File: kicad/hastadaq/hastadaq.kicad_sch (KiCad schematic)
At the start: 38 parts, among them J1 IMU via Qwiic breakout (The P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, J10 SBUS IN (RC receiver): GND, V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, J2 GAUGE BOARD LOOM (J_I2C): GND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, J3 ENC1 SPI port: MT6835 (pitch)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, J4 ENC2 SPI port: MT6835 / Orbis, J5 ENC3 SPI port: MT6835 / Orbis, J6 ENC4 SPI port: generic SPI de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, J7 SBUS servo header 3x6 (6 plug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, J8 Main supply cable (2x4): VSUP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, J9 TRIG_OUT pull-up sel., Q1 2N3904 NPN (TO-92, pin 1 E, 2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, U1 Pimoroni Pico Plus 2 (header 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, U2 Pololu D42V55F8 8.4V 5A buck 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, U3 SparkFun BabyBuck 5V (AP63357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, U4 PC817 opto (TRIG_IN)

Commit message: Schematics: fuse removed, plain headers, real parts chosen; gauge board LDO/caps; hand-off docs
- Main board: no fuse (+12V straight from the supply connector), every connector a
  plain 0.1 in header, plain test pads, FOD817A opto, chosen capacitor footprints
- Gauge board: MCP1700-3302E/TO LDO (pin 1 GND, 2 VIN, 3 VOUT), tantalum output cap,
  Vishay K-series 100 nF with 2.5 mm pitch, DNP flags on the filter caps, test points,
  pass-through loom header, redundant ADC decoupling removed
- Docs: PCB_BRIEF.md/PCB_BRIEF_GAUGE.md rewritten with a status and hand-off section,
  new PARTS_TO_SELECT.md (RS numbers, dimensions, open items), README updated,
  BabyBuck EN and ADS122C04 pull-up/address facts recorded from the data sheets

Co-Authored-By: Claude Sonnet 5.5 <noreply@anthropic.com>
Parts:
- removed F1: Fuse T3.15A 5x20mm time-delay, Fuse:Fuseholder_Clip-5x20mm_Keystone_3517_Inline_P23.11x6.76mm_D1.70mm_Horizontal, symbol HastaDAQ:Fuse
- C1: value 100uF input bulk (>=25V) -> 100uF 25V input bulk (Panasonic ECA1EM101); footprint Capacitor_THT:CP_Radial_D8.0mm_P3.50mm -> Capacitor_THT:CP_Radial_D6.3mm_P2.50mm
- C2: value 470-1000uF servo bulk (>=16V) -> 470uF 16V servo bulk (Panasonic EEUFR1C471); footprint Capacitor_THT:CP_Radial_D10.0mm_P5.00mm -> Capacitor_THT:CP_Radial_D8.0mm_P3.50mm
- C3: value 100uF 5V bulk (>=10V) -> 100uF 10V 5V bulk (RS PRO LHK 5x7); footprint Capacitor_THT:CP_Radial_D6.3mm_P2.50mm -> Capacitor_THT:CP_Radial_D5.0mm_P2.00mm
- J1: footprint HastaDAQ:Qwiic_Breakout_1x4_Socket -> Connector_PinHeader_2.54mm:PinHeader_1x04_P2.54mm_Vertical
- J3, J4, J5, J6, J8: footprint Connector_IDC:IDC-Header_2x04_P2.54mm_Vertical -> Connector_PinHeader_2.54mm:PinHeader_2x04_P2.54mm_Vertical
- TP1, TP2: footprint TestPoint:TestPoint_THTPad_D2.0mm_Drill1.0mm -> TestPoint:TestPoint_Pad_D2.0mm
- U4: value PC817 opto (TRIG_IN) -> FOD817A opto (TRIG_IN)
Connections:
- net +12V_IN is gone; now on net +12V: J8.1 (VSUPPLY), J8.8 (VSUPPLY)
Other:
- note added: "PWR_FLAG: marks nets supplied through the supply connector (+12V, GND) and the Schottky (+5V_VSYS)"
- note added: "TEST POINTS (plain 2.0 mm pads): two GND pads for a scope clip (near the supply and near the Pico). Rails and signals are probed at component leads and header pins (C1/C2/C3, D1, Pico pins 36/39)."
- note removed: "PWR_FLAG: marks nets supplied through the supply connector (+12V_IN, GND), the fuse (+12V) and the Schottky (+5V_VSYS)"
- note removed: "TEST POINTS (2.0 mm through-hole pads): two GND pads for a scope clip (near the supply and near the Pico). Rails and signals are probed at component leads and header pins (fuse clips, C5/C6/C7, D1, Pico pins 36/39)."

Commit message: Schematics: shunt-safe J9, SBUS IN on +5V with zener, 20 V max note; publish tool
- J9 TRIG_OUT pull-up select is now a 1x5 header (rails separated by PU pins) so a shunt cannot join two rails
- SBUS IN is powered from +5V (Futaba R3008SB is 4.8-7.4 V) with a 5.1 V zener clamp (D4); R14 pull-down left unfitted first (RP2350 E9)
- Supply maximum 20 V documented (C1 25 V rating); no TVS
- Gauge brief: plug-order correction, stray L1 row removed
- kicad/tools/publish.py snapshots both schematics into kicad/releases/<name>/ for PCB layout
- PDFs/PNGs re-exported

Co-Authored-By: Claude Sonnet 5.5 <noreply@anthropic.com>
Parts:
- removed J9: TRIG_OUT pull-up sel., Connector_PinHeader_2.54mm:PinHeader_2x03_P2.54mm_Vertical, symbol HastaDAQ:Header2x03_PU_SEL
- added D4: 5.1V zener (BZX55C5V1) SBUS IN clamp, Diode_THT:D_DO-35_SOD27_P7.62mm_Horizontal, symbol HastaDAQ:D_Zener
- added J9: TRIG_OUT pull-up (1x5), Connector_PinHeader_2.54mm:PinHeader_1x05_P2.54mm_Vertical, symbol HastaDAQ:Header1x05_3V3pPUp5VpPUp12V
- R14: value 10k pull-down -> 10k pull-down (DNP at first)
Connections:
- net +12V: now also J9.5 (12V)
- net +3V3: now also J9.1 (3V3)
- net +5V: now also J10.2 (V), J9.3 (5V)
- net GND: now also D4.A
- net SBUS_IN_GPIO: now also D4.K
- net TRIG_PU: now also J9.2 (PU), J9.4 (PU)
- net VSERVO: no longer J10.2 (V)
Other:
- note added: "SBUS IN: RC-receiver pass-through (plug order GND, V, SIG). V = +5V (NOT VSERVO: the Futaba R3008SB takes 4.8-7.4 V, so 8.4 V would overstress it; check any other receiver's range). SIG -> 1k -> GP1 (UART0 RX); 5.1 V zener clamps a receiver that outputs more than 5.1 V (about 100 pF at 100 kbaud: harmless). 10k pull-down R: leave UNFITTED on the first trial; RP2350 erratum E9 can hold a pin with 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"
- note added: "Shunt pins 1-2 (3V3), 2-3 (5V) or 4-5 (12V) to pull TRIG_OUT up to that rail; fit none if the receiver has its own pull-up. Pins 2 and 4 are both TRIG_PU. Fit ONE shunt only (two shunts could join rails). Pull-up current: 3.3 V ~2 mA, 5 V ~3 mA, 12 V ~7 mA (enough for a 6.5 mA opto input such as MPS4200). 24 V receivers: no jumper, add an external 24 V pull-up in the harness. 3V3 for eSync 2 high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"
- note removed: "Jumper a row (3V3 / 5V / 12V) to pull TRIG_OUT up to that rail; remove it if the receiver has its own pull-up. Pull-up current: 3.3 V ~2 mA, 5 V ~3 mA, 12 V ~7 mA (enough for a 6.5 mA opto input such as MPS4200). 24 V receivers: no jumper, add an external 24 V pull-up in the harness. 3V3 for eSync 2 high-Z ports (3.3 V max)."
- note removed: "SBUS IN: RC-receiver pass-through (plug order GND, V, SIG). V = VSERVO 8.4 V -- check the receiver's max supply. SIG -> 1k -> GP1 (UART0 RX), 10k to GND."

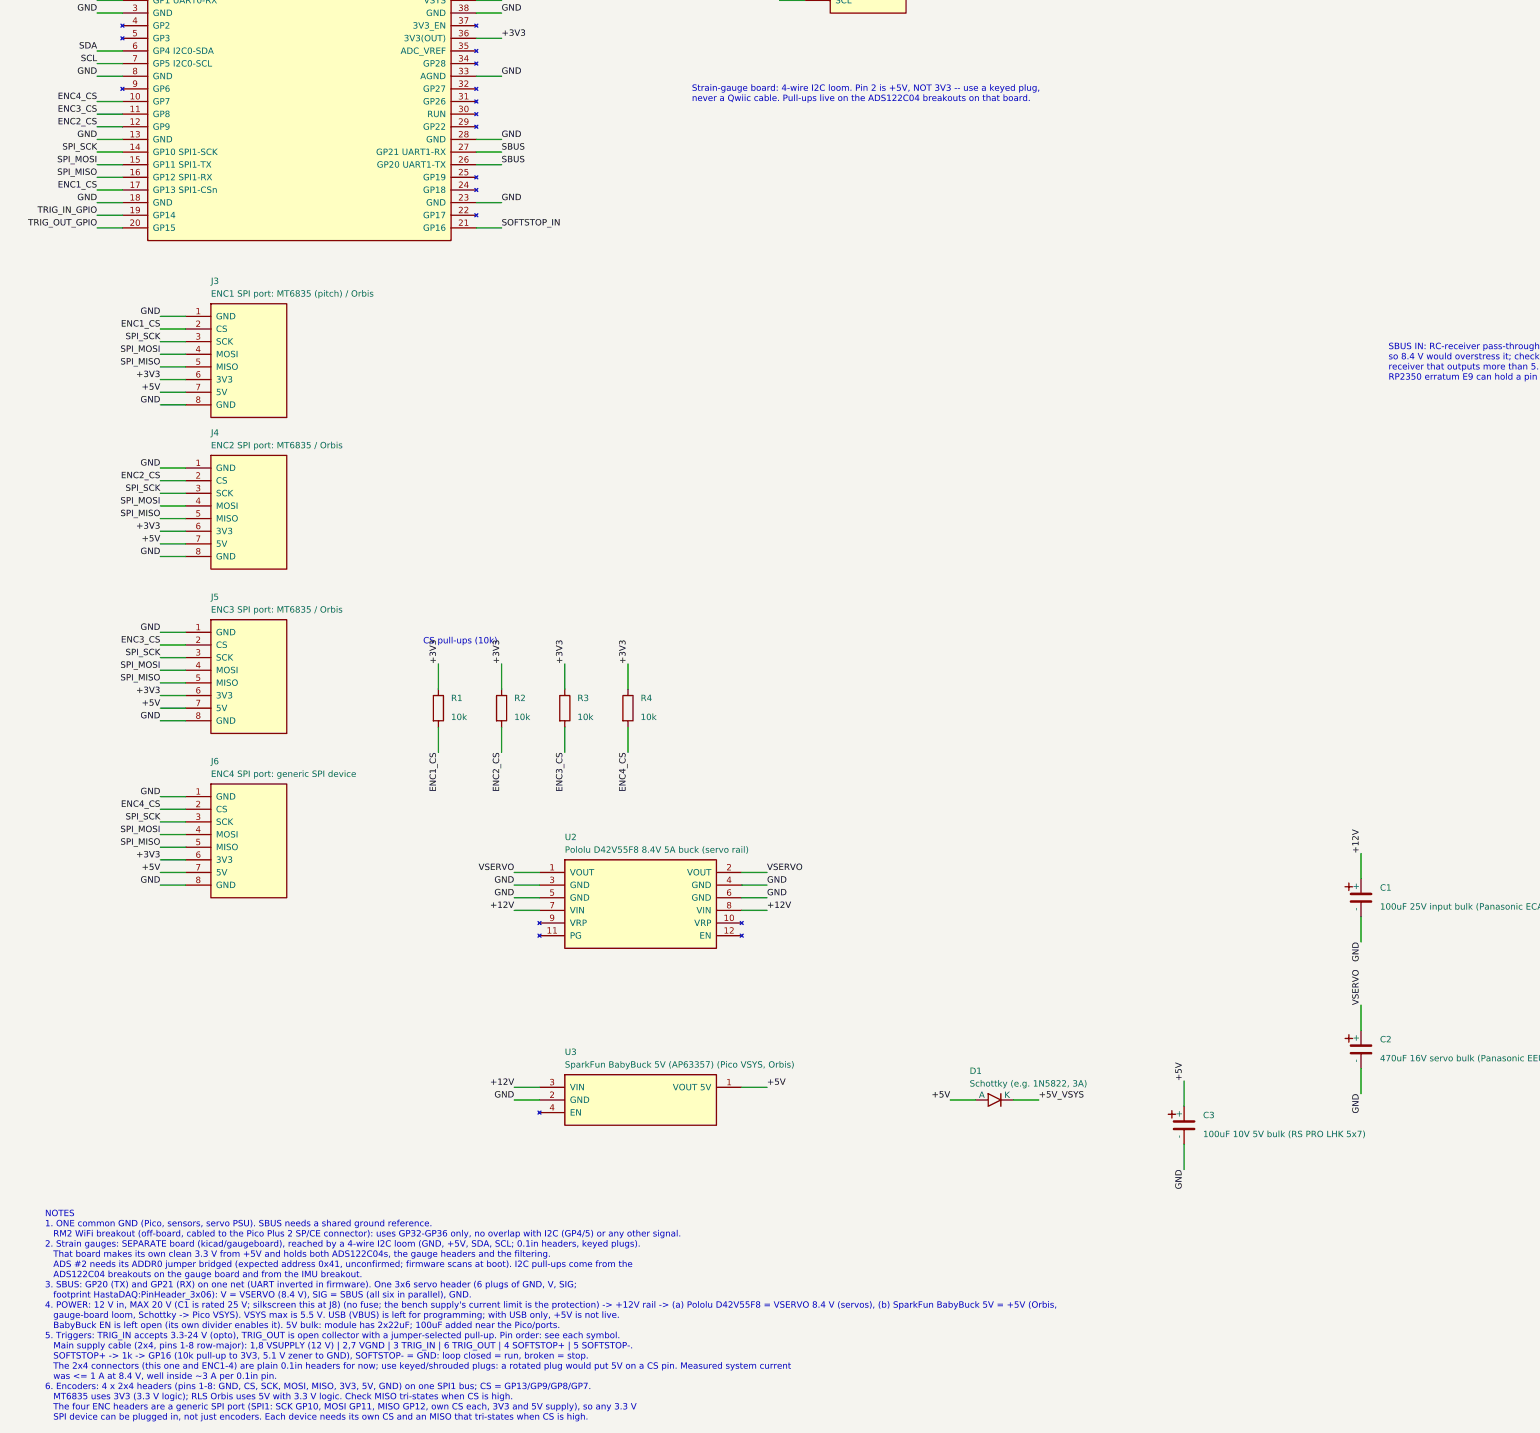
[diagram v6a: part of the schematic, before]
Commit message: Main board: RM08 SSI encoders, SSI firmware driver, placed and routed PCB
Schematic: two RLS RM08 SSI headers (J6, J11; shared clock GP17, data GP18/GP19),
ENC4 SPI port removed, diode pin numbering fixed. Firmware: PIO SSI driver
(Rm08Ssi), 84-byte sample with extra encoder channels, MATLAB DaqData update.

PCB: release 20261027-2346-rev-a-ssi, hand placement by the owner, routed with
the new grid router (route_main.py, grid_router.py): 2.0 mm VSERVO/+12V bars,
GND pours, DRC clean apart from cosmetic silk warnings. Pololu mounting holes
removed and Pico antenna keep-out trimmed 3 mm on this board only.

Layout tools: grid_router, route_main, solid_gnd_pads, trim_fp_keepout,
check_pad_nets, main_initial_placement (historical), tidy_silk two-sided,
set_pcbway_rules --ignore. Docs and READMEs updated.

Co-Authored-By: Claude Sonnet 5.5 <noreply@anthropic.com>
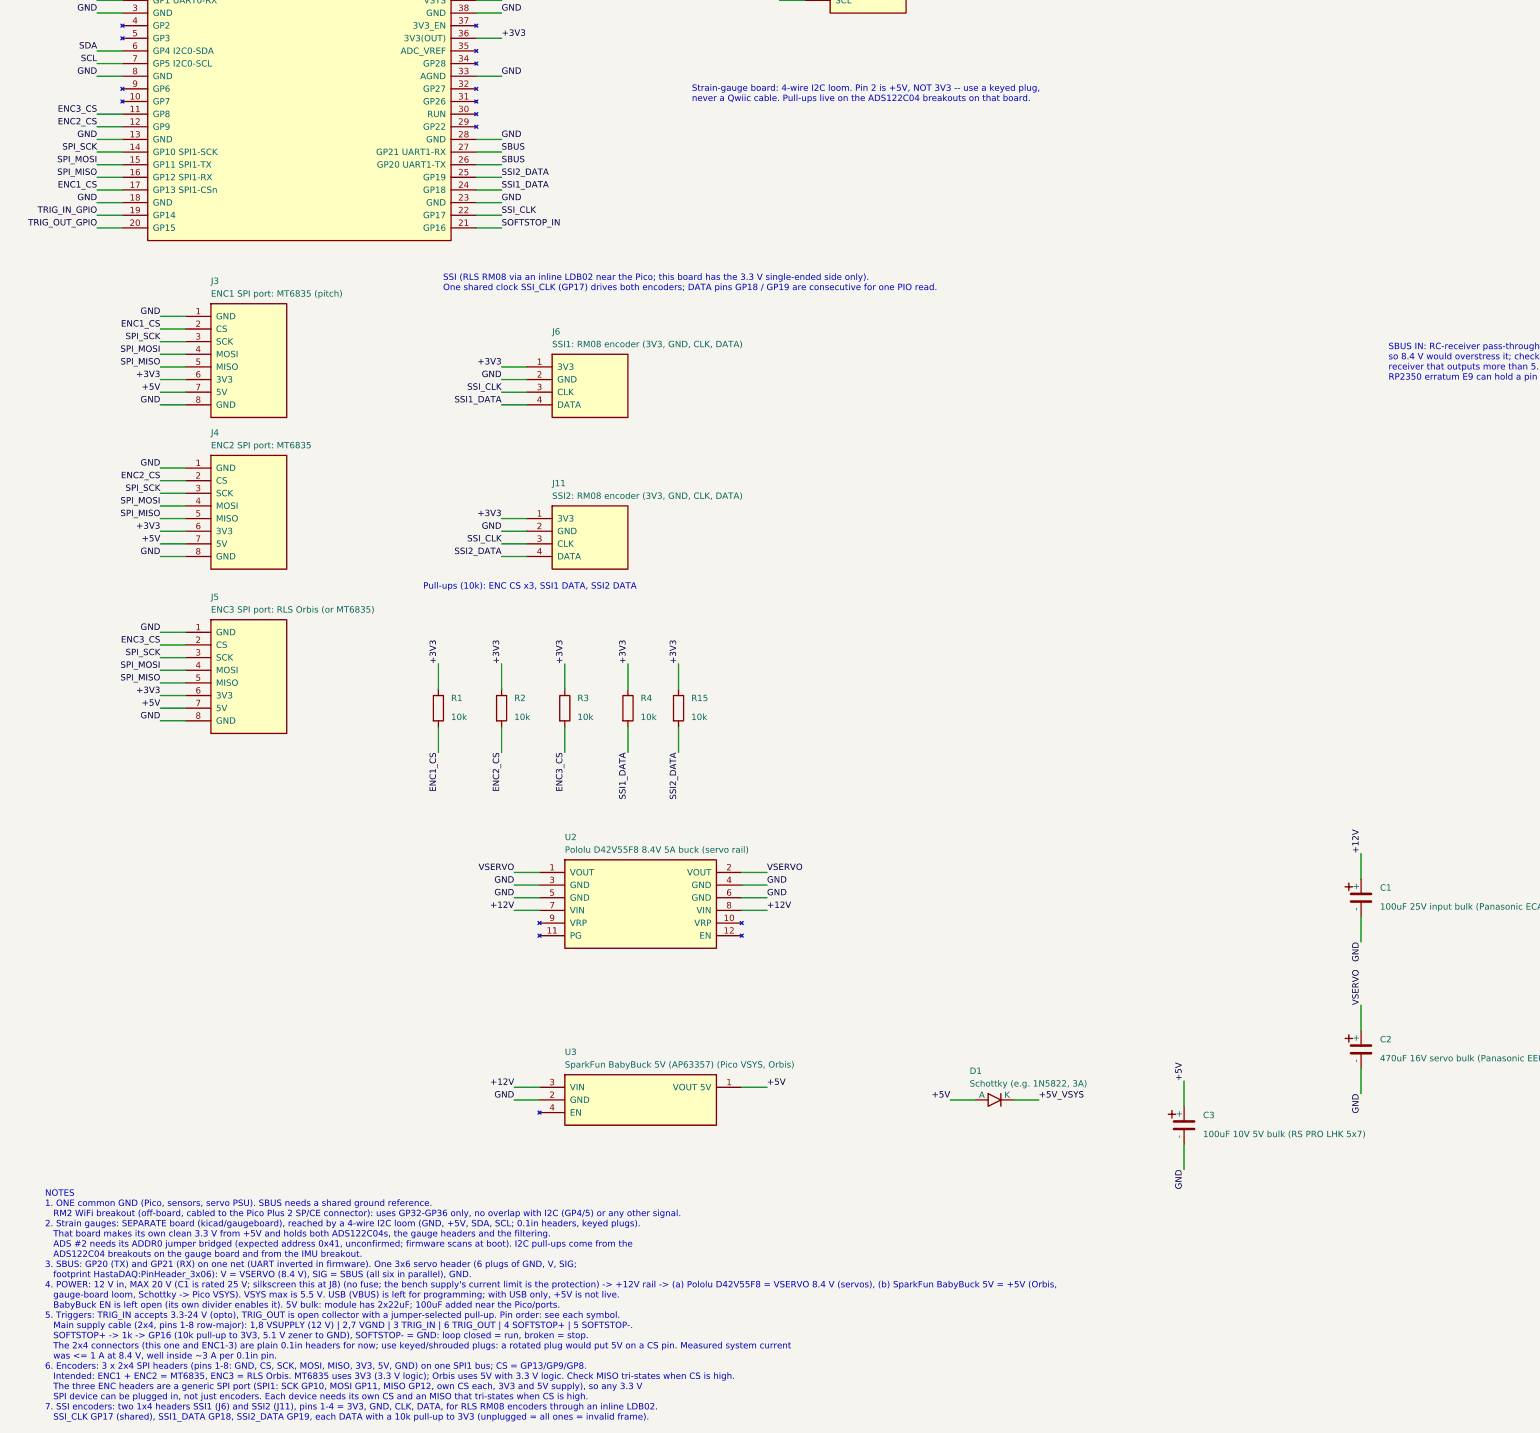
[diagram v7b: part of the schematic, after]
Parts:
- removed J6: ENC4 SPI port: generic SPI device, Connector_PinHeader_2.54mm:PinHeader_2x04_P2.54mm_Vertical, symbol HastaDAQ:Header2x04_GNDpCSpSCKpMOSIpMISOp3V3p5VpGND
- added J11: SSI2: RM08 encoder (3V3, GND, CLK, DATA), Connector_PinHeader_2.54mm:PinHeader_1x04_P2.54mm_Vertical, symbol HastaDAQ:Header1x04_3V3pGNDpCLKpDATA
- added J6: SSI1: RM08 encoder (3V3, GND, CLK, DATA), Connector_PinHeader_2.54mm:PinHeader_1x04_P2.54mm_Vertical, symbol HastaDAQ:Header1x04_3V3pGNDpCLKpDATA
- added R15: 10k, Resistor_THT:R_Axial_DIN0207_L6.3mm_D2.5mm_P7.62mm_Horizontal, symbol HastaDAQ:R
- J3: value ENC1 SPI port: MT6835 (pitch) / Orbis -> ENC1 SPI port: MT6835 (pitch)
- J4: value ENC2 SPI port: MT6835 / Orbis -> ENC2 SPI port: MT6835
- J5: value ENC3 SPI port: MT6835 / Orbis -> ENC3 SPI port: RLS Orbis (or MT6835)
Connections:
- net +3V3: now also J11.1 (3V3), J6.1 (3V3), R15.1
- net +5V: now also D1.2 (A); no longer D1.A
- net +5V_VSYS: now also D1.1 (K); no longer D1.K
- net GND: now also D2.2 (A), D3.2 (A), D4.2 (A), J11.2 (GND), J6.2 (GND); no longer D2.A, D3.A, D4.A
- net SBUS_IN_GPIO: now also D4.1 (K); no longer D4.K
- net SOFTSTOP_IN: now also D2.1 (K); no longer D2.K
- net TRIG_IN_LED: now also D3.1 (K); no longer D3.K
- net SSI_CLK: now reaches U1.22 (GP17)
- net SSI_CLK: now also J11.3 (CLK), J6.3 (CLK)
- net SSI1_DATA: now reaches U1.24 (GP18)
- net SSI1_DATA: now also R4.2, J6.4 (DATA)
- net SSI2_DATA: now reaches U1.25 (GP19)
- net SSI2_DATA: now also J11.4 (DATA), R15.2
- net ENC4_CS: no longer names the net of U1.10 (GP7)
- net ENC4_CS: no longer R4.2
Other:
- note added: "Pull-ups (10k): ENC CS x3, SSI1 DATA, SSI2 DATA"
- note added: "SSI (RLS RM08 via an inline LDB02 near the Pico; this board has the 3.3 V single-ended side only). One shared clock SSI_CLK (GP17) drives both encoders; DATA pins GP18 / GP19 are consecutive for one PIO read."
- note removed: "CS pull-ups (10k)"
